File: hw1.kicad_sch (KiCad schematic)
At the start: 26 parts, among them J1 USB_C_Receptacle_USB2.0_16P, M1 Stepper_Motor, SW1 RotaryEncoder_Switch, SW2 SW_Back, SW3 SW_Bolus, SW4 SW_Settings, SW5 SW_Push, SW6 SW_Push, U4 USBLC6-2SC6, U6 ESP32-C6-WROOM-1

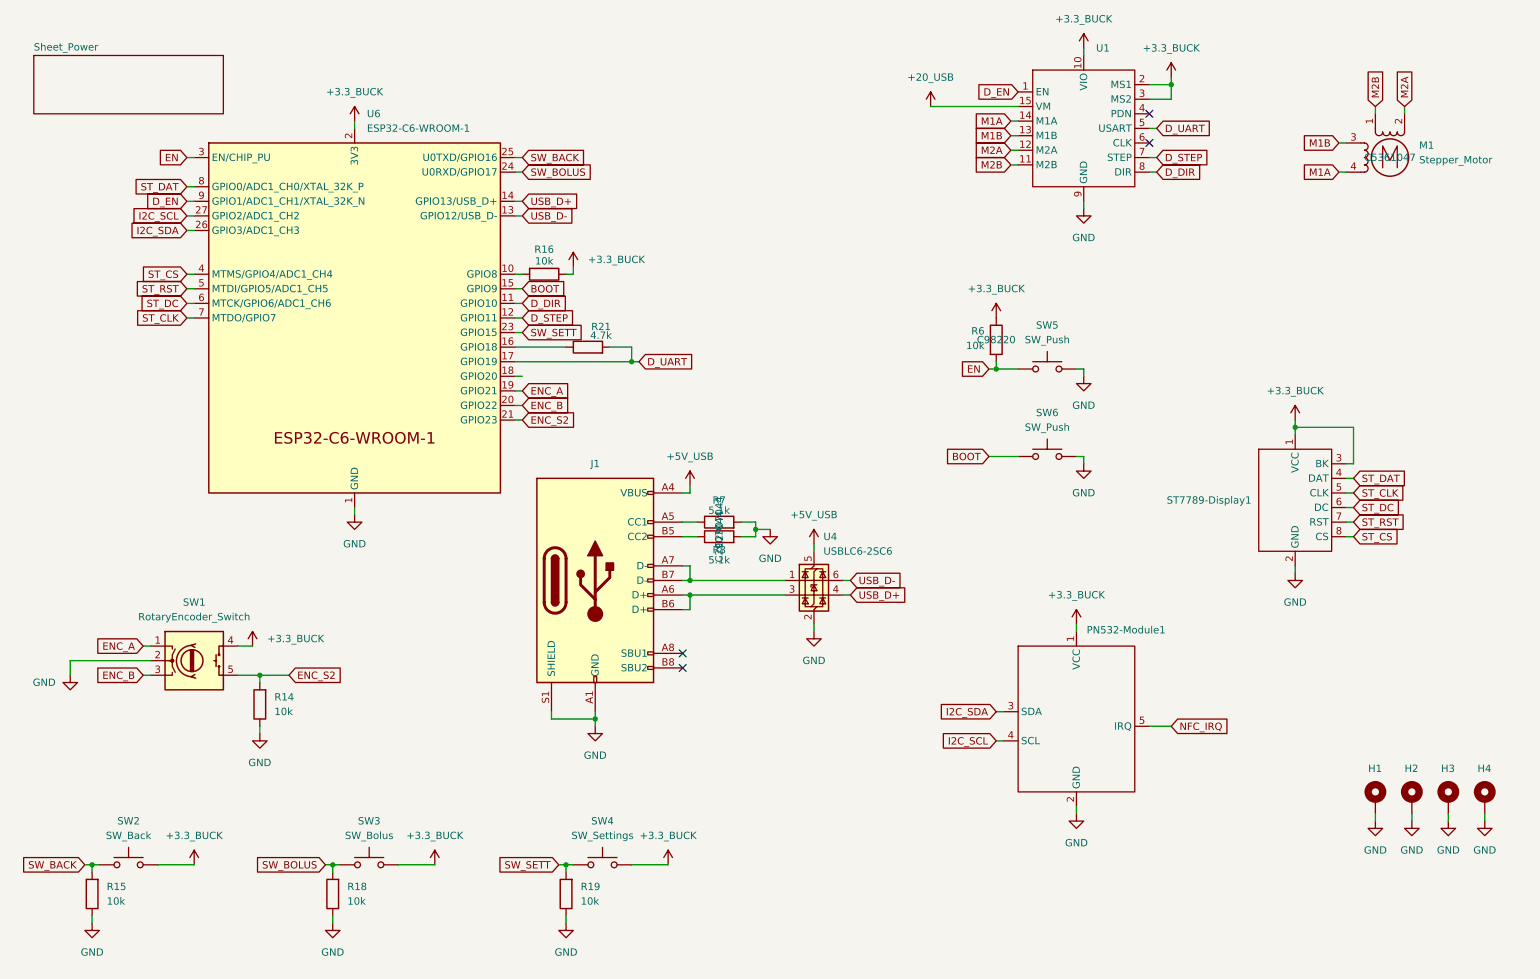
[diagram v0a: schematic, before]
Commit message: Added LCSC codes, swapped extended components for basic ones, fixed labels and tidied schematics.
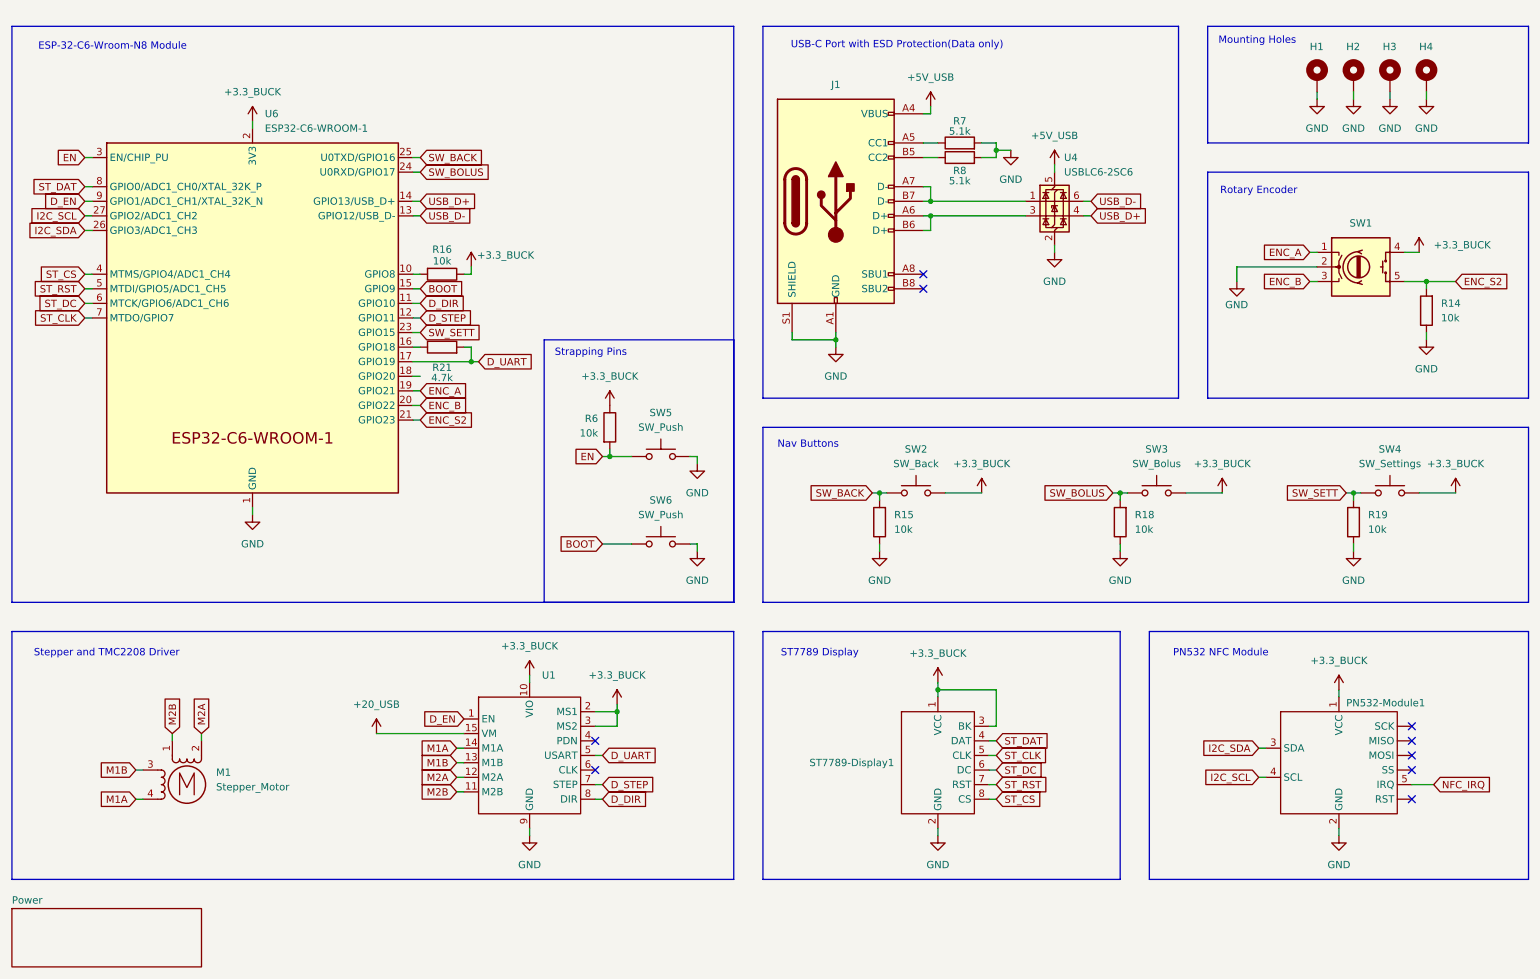
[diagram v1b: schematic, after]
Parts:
- J1: LCSC C52209111 -> C2765186
- R14, R15, R16, R18, R19, R6: LCSC C98220 -> C25804
- R7, R8: LCSC C2907044 -> C23186
- U4: LCSC (none) -> C7519
- U6: LCSC (none) -> C5366877
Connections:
- no-connect marks 4 -> 9
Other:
- sheet Sheet_Power renamed Power
- note added: "ESP-32-C6-Wroom-N8 Module"
- note added: "Mounting Holes"
- note added: "Nav Buttons"
- note added: "PN532 NFC Module"
- note added: "Rotary Encoder"
- note added: "ST7789 Display"
- note added: "Stepper and TMC2208 Driver"
- note added: "Strapping Pins"
- note added: "USB-C Port with ESD Protection(Data only)"
- moved on the sheet: H1, H2, H3, H4, J1, M1, R14, R15, R16, R18, R19, R21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
